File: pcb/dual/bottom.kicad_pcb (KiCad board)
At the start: 2 copper layers, 242.5 x 87.9 mm, 10 parts

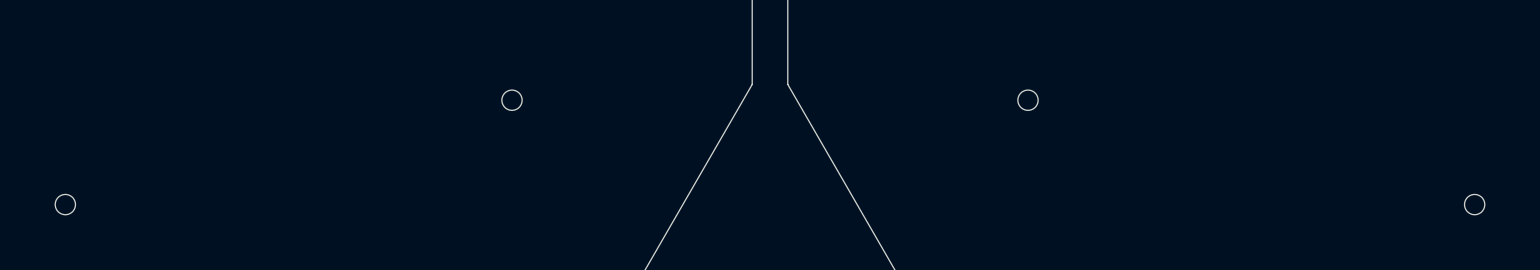
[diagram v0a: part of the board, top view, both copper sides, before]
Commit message: Standoffs in a rectangle, screw holes back in the switch plate
The standoff stack is holykeebs': a spacer through the main board's 3.1 mm
hole, a top screw through the switch plate, a bottom screw through the
bottom plate; the main board hangs from the switches. The plate's screw
holes, removed early on as supposed OLED-cover holes, are back (2.1 mm)
over every standoff.

Per half, four standoffs sit at four-key centres forming a 54 x 34 mm
rectangle (pinky|ring and index|inner index, top and bottom) and one at
the thumbs. The logo's standoff moves to the index bottom, so the logo
carries a solid 7 mm dot on board and plate. README: hardware (5 mm round
spacers; small-head top screws where four keys meet), assembly and feet.
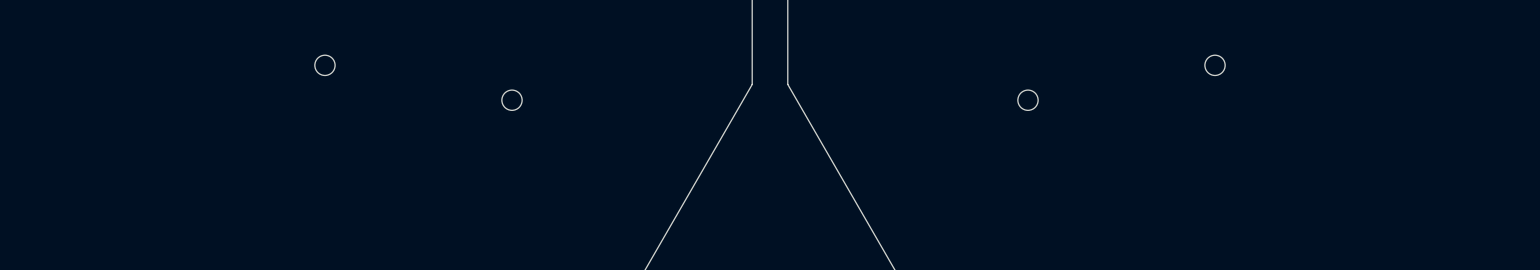
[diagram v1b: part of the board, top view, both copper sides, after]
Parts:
- moved H2 32.0 mm to (107.5, 107.2)
- moved H9 32.0 mm to (204.2, 107.2)
